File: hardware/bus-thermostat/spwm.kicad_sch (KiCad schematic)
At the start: 28 parts

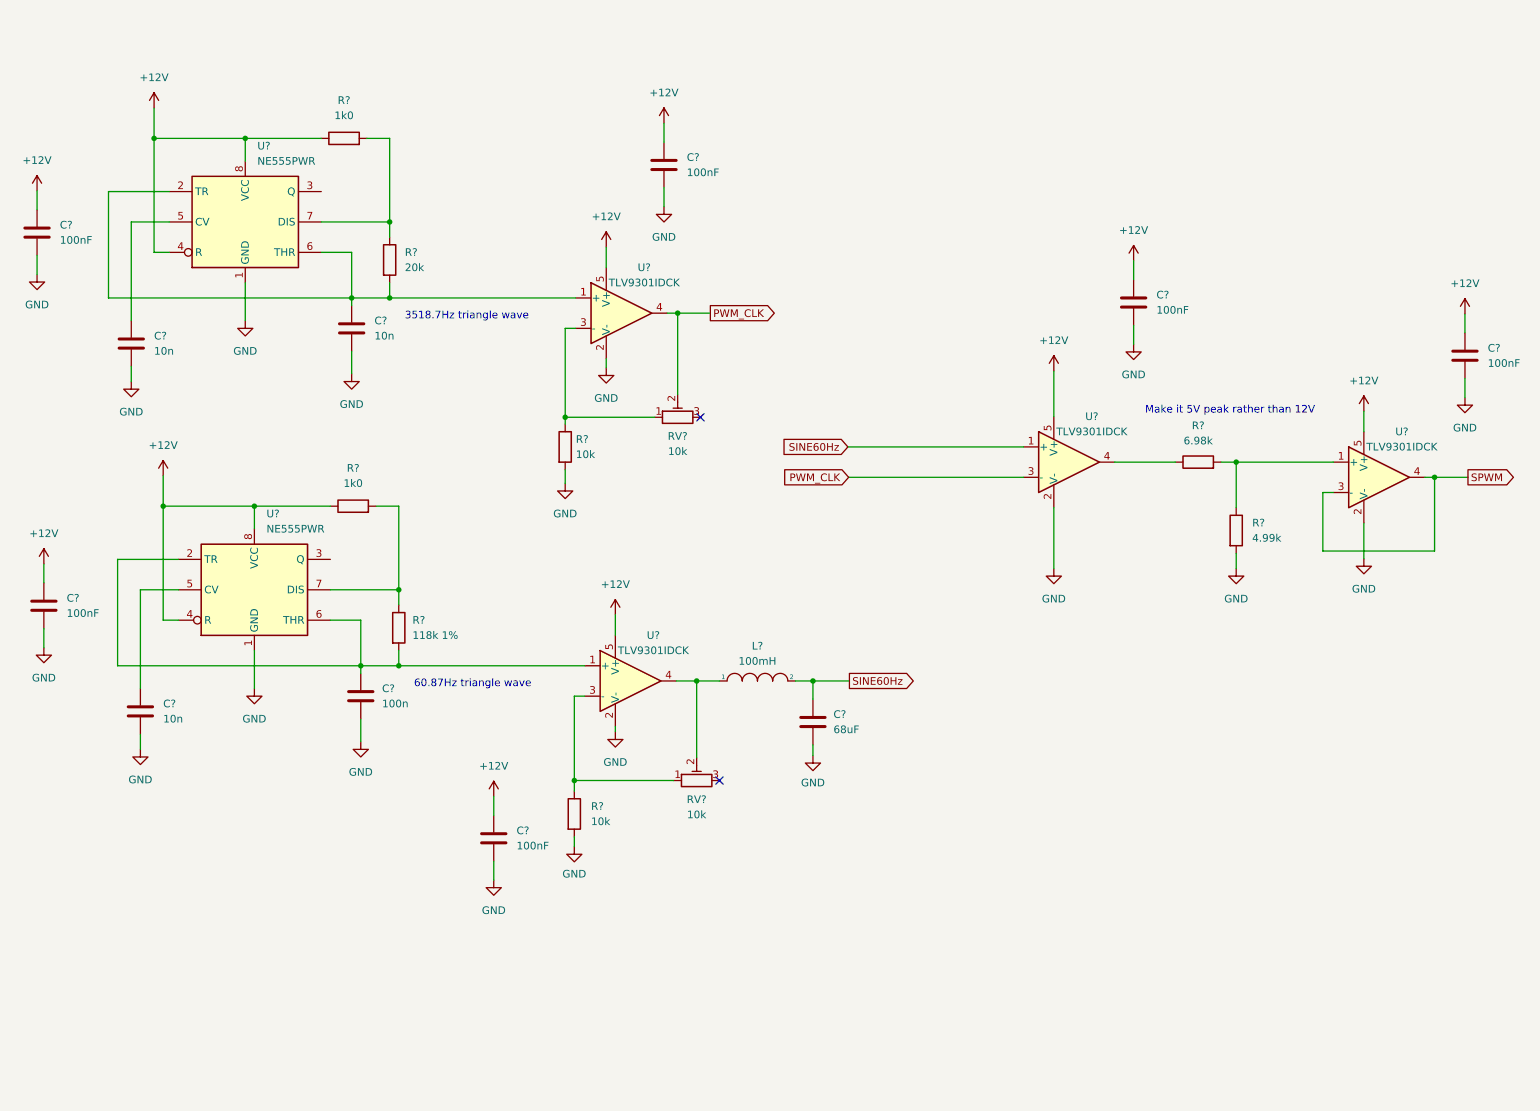
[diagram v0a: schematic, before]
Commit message: Redid the 24VAC path entirely.
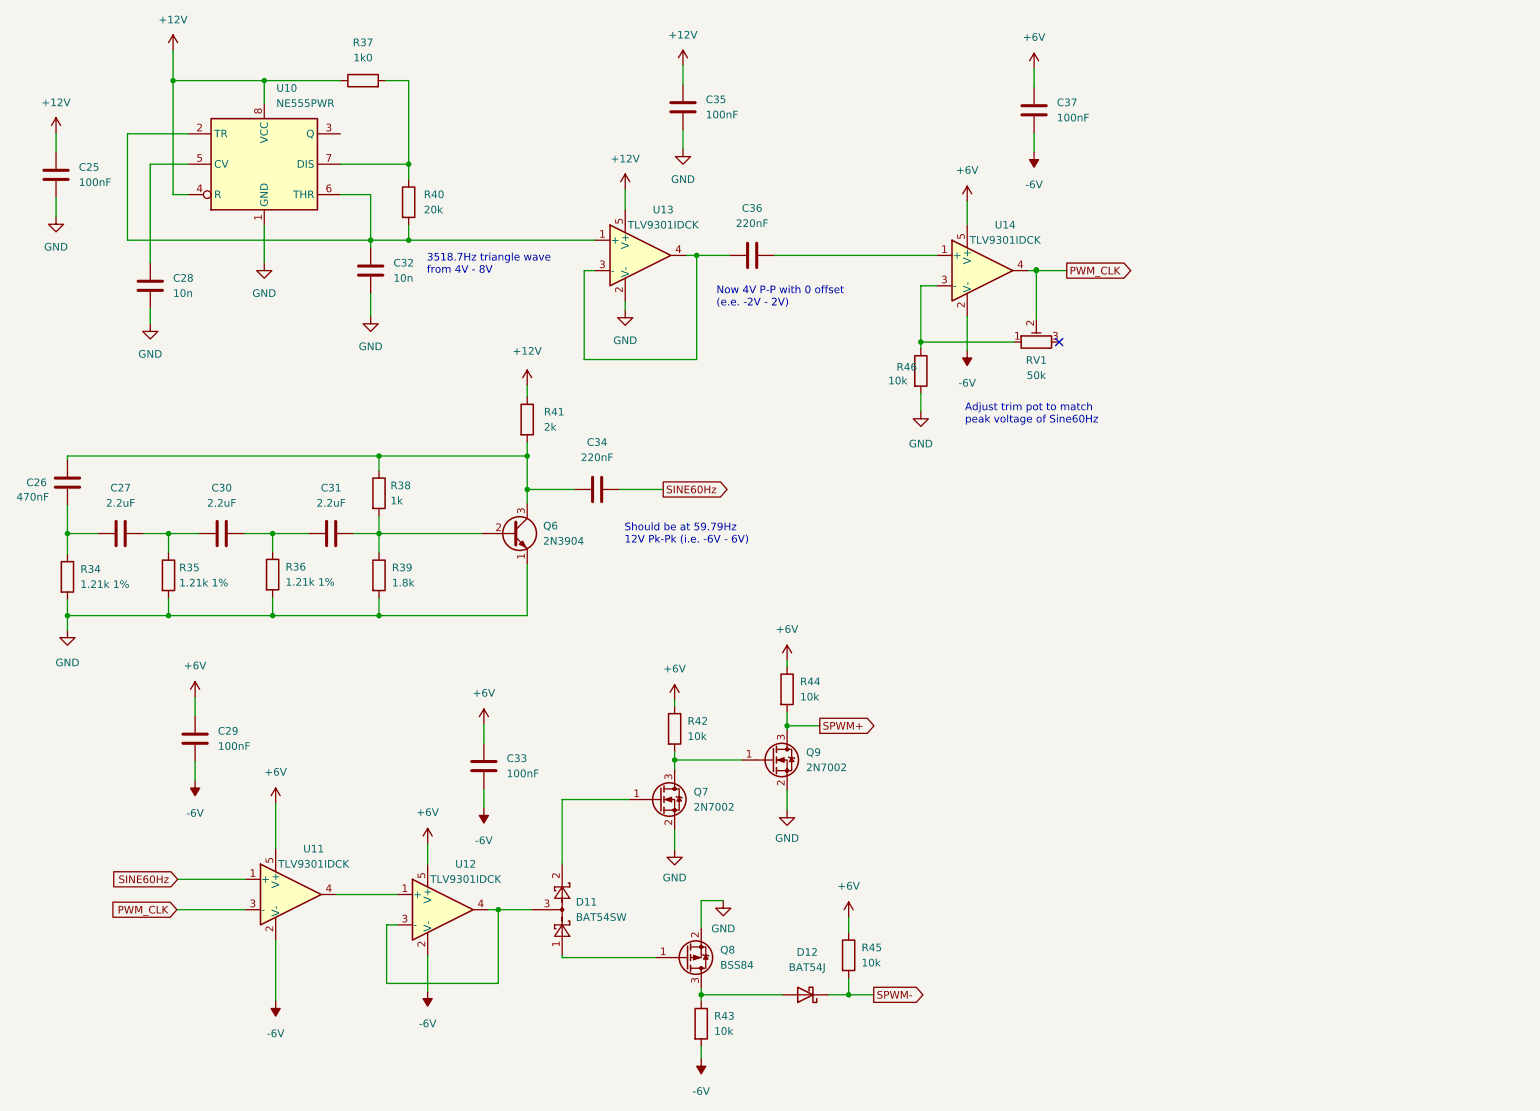
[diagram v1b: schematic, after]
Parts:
- removed C? (x4): 100nF, symbol Device:C
- removed C?: 100n, symbol Device:C
- removed C?: 10n, symbol Device:C
- removed C?: 68uF, symbol Device:C
- removed L?: 100mH, symbol pspice:INDUCTOR
- removed R?: 118k 1%, symbol Device:R
- removed R?: 6.98k, symbol Device:R
- removed R? (x2): 10k, symbol Device:R
- removed R?: 1k0, symbol Device:R
- removed R?: 4.99k, symbol Device:R
- removed RV? (x2): 10k, symbol Device:R_Potentiometer_Trim
- removed U?: NE555PWR, Package_SO:TSSOP-8_4.4x3mm_P0.65mm, symbol Timer:NE555P
- removed U?: TLV9301IDCK, Package_TO_SOT_SMD:SOT-353_SC-70-5, symbol Amplifier_Operational:TLV9001IDCK
- added C26: 470nF, symbol Device:C
- added C27, C30, C31: 2.2uF, symbol Device:C
- added C29, C33, C37: 100nF, symbol Device:C
- added C34, C36: 220nF, symbol Device:C
- added D11: BAT54SW, Package_TO_SOT_SMD:SOT-323_SC-70, symbol Diode:BAT54SW
- added D12: BAT54J, Diode_SMD:D_SOD-323F, symbol Diode:BAT54J
- added Q6: 2N3904, Package_TO_SOT_THT:TO-92_Inline, symbol Transistor_BJT:2N3904
- added Q7, Q9: 2N7002, Package_TO_SOT_SMD:SOT-23, symbol Transistor_FET:2N7002
- added Q8: BSS84, Package_TO_SOT_SMD:SOT-23, symbol Transistor_FET:BSS84
- added R34, R35, R36: 1.21k 1%, symbol Device:R
- added R38: 1k, symbol Device:R
- added R39: 1.8k, symbol Device:R
- added R41: 2k, symbol Device:R
- added R42, R43, R44, R45, R46: 10k, symbol Device:R
- added RV1: 50k, symbol Device:R_Potentiometer_Trim
- added U14: TLV9301IDCK, Package_TO_SOT_SMD:SOT-353_SC-70-5, symbol Amplifier_Operational:TLV9001IDCK
- gave numbers to parts that had none: 10
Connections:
- net +12V: now also R41.1; no longer U11.5 (V+), U12.5 (V+)
- net GND: now also Q6.1 (E), Q7.2 (S), Q8.2 (S), Q9.2 (S), R34.2, R35.2, R36.2, R39.2, R46.2; no longer U11.2 (V-), U12.2 (V-)
- net PWM_CLK: now also RV1.2, U14.4; no longer U13.4
- net SINE60Hz: now also C34.2
- net at U13.3 (-): now also U13.4, C36.1
- net at U11.4: now also U12.1 (+)
- net SPWM: no longer names the net of U12.3 (-), U12.4
- net SPWM: now also D11.3
- new net: C26.2, C27.1, R34.1
- new net: D12.2 (A), Q8.3 (D), R43.1
- new net: D11.1, Q8.1 (G)
- new net: C36.2, U14.1 (+)
- new net: R46.1, RV1.1, U14.3 (-)
- new net: Q7.3 (D), Q9.1 (G), R42.2
- new net: D11.2, Q7.1 (G)
- new net: C31.2, Q6.2 (B), R38.2, R39.1
- new net: C30.2, C31.1, R36.1
- new net: C26.1, C34.1, Q6.3 (C), R38.1, R41.2
- new net: C27.2, C30.1, R35.1
- new net +6V: C29.1, C33.1, C37.1, R42.1, R44.1, R45.1, U11.5 (V+), U12.5 (V+), U14.5 (V+)
- new net -6V: C29.2, C33.2, C37.2, R43.2, U11.2 (V-), U12.2 (V-), U14.2 (V-)
- new net SPWM+: Q9.3 (D), R44.2
- new net SPWM-: D12.1 (K), R45.2
- no-connect marks 2 -> 1
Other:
- note added: "3518.7Hz triangle wave from 4V - 8V"
- note added: "Adjust trim pot to match peak voltage of Sine60Hz"
- note added: "Now 4V P-P with 0 offset (e.e. -2V - 2V)"
- note added: "Should be at 59.79Hz 12V Pk-Pk (i.e. -6V - 6V)"
- note removed: "3518.7Hz triangle wave"
- note removed: "60.87Hz triangle wave"
- note removed: "Make it 5V peak rather than 12V"
- moved on the sheet: C25, C28, C32, C35, R37, R40, U10, U11, U12, U13

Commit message: First rev of thermostat firmware
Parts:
- added C?: 470nF, symbol Device:C
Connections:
- net at C26.2, C27.1, R34.1: now also C?.2
- new net OSC_PRIME: C?.1
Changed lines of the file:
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@@
+    (stroke (width 0) (type default) (color 0 0 0 0))
+  )
+  (wire (pts (xy 13.716 103.124) (xy 22.987 103.124))
     (stroke (width 0) (type default) (color 0 0 0 0))
   )
@@
     (stroke (width 0) (type default) (color 0 0 0 0))
   )
+  (wire (pts (xy 35.052 84.963) (xy 39.751 84.963))
+    (stroke (width 0) (type default) (color 0 0 0 0))
+  )
   (wire (pts (xy 124.46 140.97) (xy 135.636 140.97))
     (stroke (width 0) (type default) (color 0 0 0 0))
@@
     (stroke (width 0) (type default) (color 0 0 0 0))
   )
+  (wire (pts (xy 13.716 84.963) (xy 13.716 103.124))
+    (stroke (width 0) (type default) (color 0 0 0 0))
+  )
   (wire (pts (xy 33.02 54.102) (xy 73.66 54.102))
     (stroke (width 0) (type default) (color 0 0 0 0))
@@
   )
   (wire (pts (xy 43.18 41.402) (xy 36.83 41.402))
+    (stroke (width 0) (type default) (color 0 0 0 0))
+  )
+  (wire (pts (xy 27.432 84.963) (xy 13.716 84.963))
     (stroke (width 0) (type default) (color 0 0 0 0))
   )
@@
   (text "Should be at 59.79Hz\n12V Pk-Pk (i.e. -6V - 6V)" (at 116.078 105.029 0)
     (effects (font (size 1.27 1.27)) (justify left bottom))
+  )
+  (global_label "OSC_PRIME" (shape input) (at 39.751 84.963 0) (fields_autoplaced)
+    (effects (font (size 1.27 1.27)) (justify left))
+    (property "Intersheet References" "${INTERSHEET_REFS}" (id 0) (at 52.687 85.0424 0)
+      (effects (font (size 1.27 1.27)) (justify left) hide)
+    )
   )
   (global_label "PWM_CLK" (shape output) (at 189.992 59.182 0) (fields_autoplaced)
@@
     (pin "1")
   )
+  (symbol (lib_id "Device:C") (at 31.242 84.963 270) (mirror x) (unit 1)
+    (in_bom yes) (on_board yes)
+    (property "Reference" "C?" (id 0) (at 31.242 78.105 90)
+      (effects (font (size 1.27 1.27)) (justify right))
+    )
+    (property "Value" "470nF" (id 1) (at 33.782 80.645 90)
+      (effects (font (size 1.27 1.27)) (justify right))
+    )
+    (property "Footprint" "" (id 2) (at 27.432 83.9978 0)
+      (effects (font (size 1.27 1.27)) hide)
+    )
+    (property "Datasheet" "~" (id 3) (at 31.242 84.963 0)
+      (effects (font (size 1.27 1.27)) hide)
+    )
+    (pin "1")
+    (pin "2")
+  )
   (symbol (lib_id "power:+6V") (at 44.323 130.429 0) (unit 1)
